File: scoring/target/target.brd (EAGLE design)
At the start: 31.7 x 14.9 mm, 11 parts, among them J1 AVRISP6_COMPACT, U1 ATTINY85-20SU

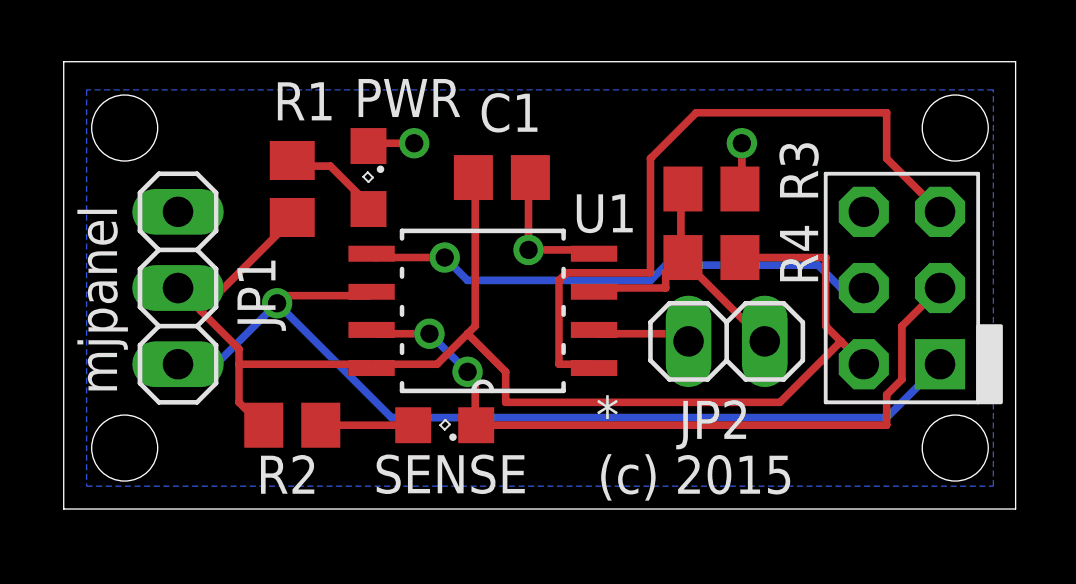
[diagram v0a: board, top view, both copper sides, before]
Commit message: Update panel board with piezo load resistors.
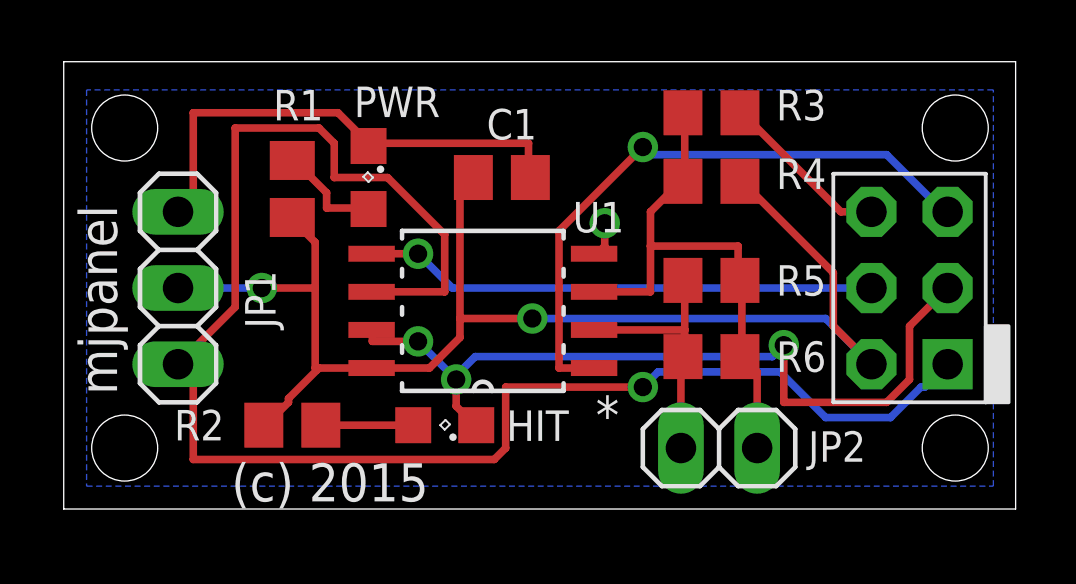
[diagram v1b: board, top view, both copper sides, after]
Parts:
- added R5: DNP, rcl:R0805
- added R6: 100, rcl:R0805
- moved JP2 3.57 mm to (21.8, 2.03)
- moved R3 2.54 mm to (21.6, 13.2)
- moved R4 2.54 mm to (21.6, 10.9)
- moved J1 0.25 mm to (28.2, 7.37)
- renumbered SENSE to HIT
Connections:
- net N$3: now also R5.1, R6.1
- net N$6: now also R5.2, R6.2
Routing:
- net N$8: track 32.0 -> 55.2 mm
- net GND: track 7.86 -> 23.4 mm, vias 3 -> 1
- net N$3: track 10.1 -> 18.5 mm
- net N$6: track 3.46 -> 8.80 mm
- net N$2: track 23.5 -> 20.7 mm, vias 0 -> 1
- net N$4: track 24.7 -> 27.0 mm, vias 2 -> 3
- net VCC: track 45.4 -> 45.7 mm, vias 0 -> 2
